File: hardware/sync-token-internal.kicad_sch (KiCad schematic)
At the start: 4 parts, among them U13 74AHC74, U18 74LVC2G125

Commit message: Switch part number for flip-flops
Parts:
- U13: JLCPCB Part Number C71900 -> C8179; Mouser Part Number 771-AHCPW118 -> 595-SN74AHC74PWR; Part Number 74AHC74PW,118 -> SN74AHC74PWR
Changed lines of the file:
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@@
 			)
 		)
-		(property "Datasheet" "https://www.mouser.com/datasheet/2/916/74AHC_AHCT74-2937188.pdf"
+		(property "Datasheet" "https://www.ti.com/lit/gpn/sn74ahc74"
 			(at 52.07 144.78 0)
 			(effects
@@
 			)
 		)
-		(property "Mouser Part Number" "771-AHCPW118"
+		(property "Mouser Part Number" "595-SN74AHC74PWR"
 			(at 52.07 144.78 0)
 			(effects
@@
 			)
 		)
-		(property "Part Number" "74AHC74PW,118"
+		(property "Part Number" "SN74AHC74PWR"
 			(at 52.07 144.78 0)
 			(effects
@@
 			)
 		)
-		(property "JLCPCB Part Number" "C71900"
+		(property "JLCPCB Part Number" "C8179"
 			(at 52.07 144.78 0)
 			(effects
@@
 			)
 		)
-		(property "Datasheet" "https://www.mouser.com/datasheet/2/916/74AHC_AHCT74-2937188.pdf"
+		(property "Datasheet" "https://www.ti.com/lit/gpn/sn74ahc74"
 			(at 187.96 111.76 0)
 			(effects
@@
 			)
 		)
-		(property "Mouser Part Number" "771-AHCPW118"
-			(at 187.96 111.76 0)
-			(effects
-				(font
-					(size 1.27 1.27)
-				)
-				(hide yes)
-			)
-		)
-		(property "Part Number" "74AHC74PW,118"
-			(at 187.96 111.76 0)
-			(effects
-				(font
-					(size 1.27 1.27)
-				)
-				(hide yes)
-			)
-		)
-		(property "JLCPCB Part Number" "C71900"
+		(property "Mouser Part Number" "595-SN74AHC74PWR"
+			(at 187.96 111.76 0)
+			(effects
+				(font
+					(size 1.27 1.27)
+				)
+				(hide yes)
+			)
+		)
+		(property "Part Number" "SN74AHC74PWR"
+			(at 187.96 111.76 0)
+			(effects
+				(font
+					(size 1.27 1.27)
+				)
+				(hide yes)
+			)
+		)
+		(property "JLCPCB Part Number" "C8179"
 			(at 187.96 111.76 0)
 			(effects
@@
 			)
 		)
-		(property "Datasheet" "https://www.mouser.com/datasheet/2/916/74AHC_AHCT74-2937188.pdf"
+		(property "Datasheet" "https://www.ti.com/lit/gpn/sn74ahc74"
 			(at 53.34 93.98 0)
 			(effects
@@
 			)
 		)
-		(property "Mouser Part Number" "771-AHCPW118"
-			(at 53.34 93.98 0)
-			(effects
-				(font
-					(size 1.27 1.27)
-				)
-				(hide yes)
-			)
-		)
-		(property "Part Number" "74AHC74PW,118"
-			(at 53.34 93.98 0)
-			(effects
-				(font
-					(size 1.27 1.27)
-				)
-				(hide yes)
-			)
-		)
-		(property "JLCPCB Part Number" "C71900"
-			(at 53.34 93.98 0)
-			(effects
+		(property "Mouser Part Number" "595-SN74AHC74PWR"
+			(at 53.34 93.98 0)
+			(effects
+				(font
+					(size 1.27 1.27)
+				)
+				(hide yes)
+			)
+		)
+		(property "Part Number" "SN74AHC74PWR"
+			(at 53.34 93.98 0)
+			(effects
+				(font
+					(size 1.27 1.27)
+				)
+				(hide yes)
+			)
+		)
+		(property "JLCPCB Part Number" "C8179"
+			(at 53.34 93.98 0)
+			(effects

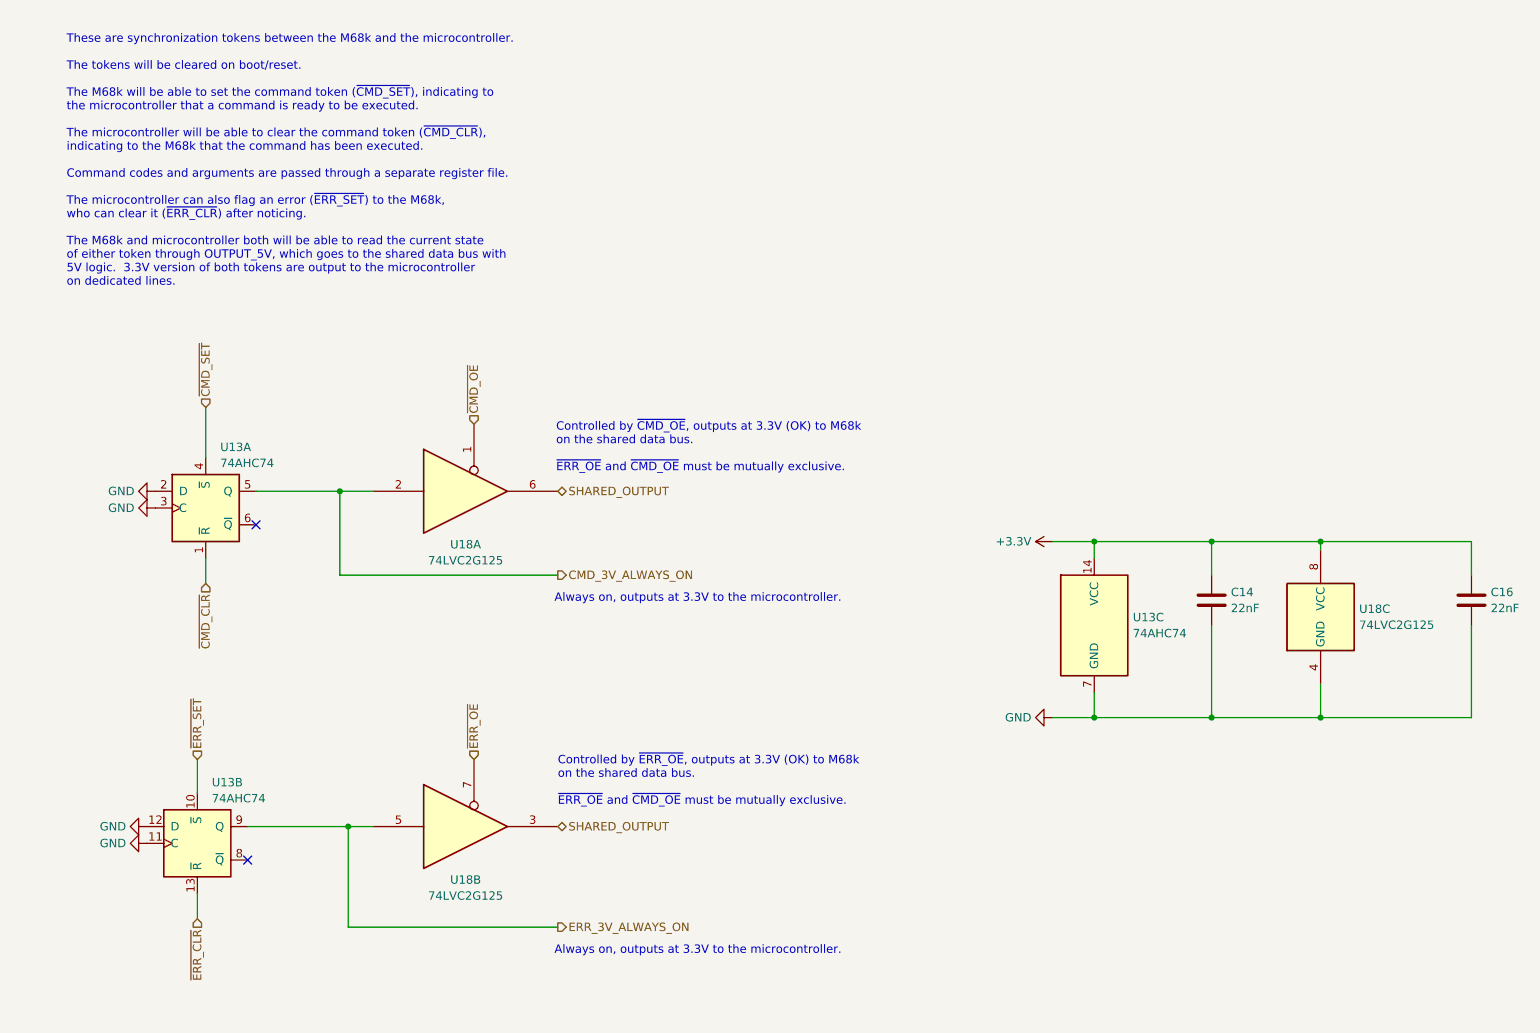
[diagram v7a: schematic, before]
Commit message: Move microcontroller board design into shareable subsheet
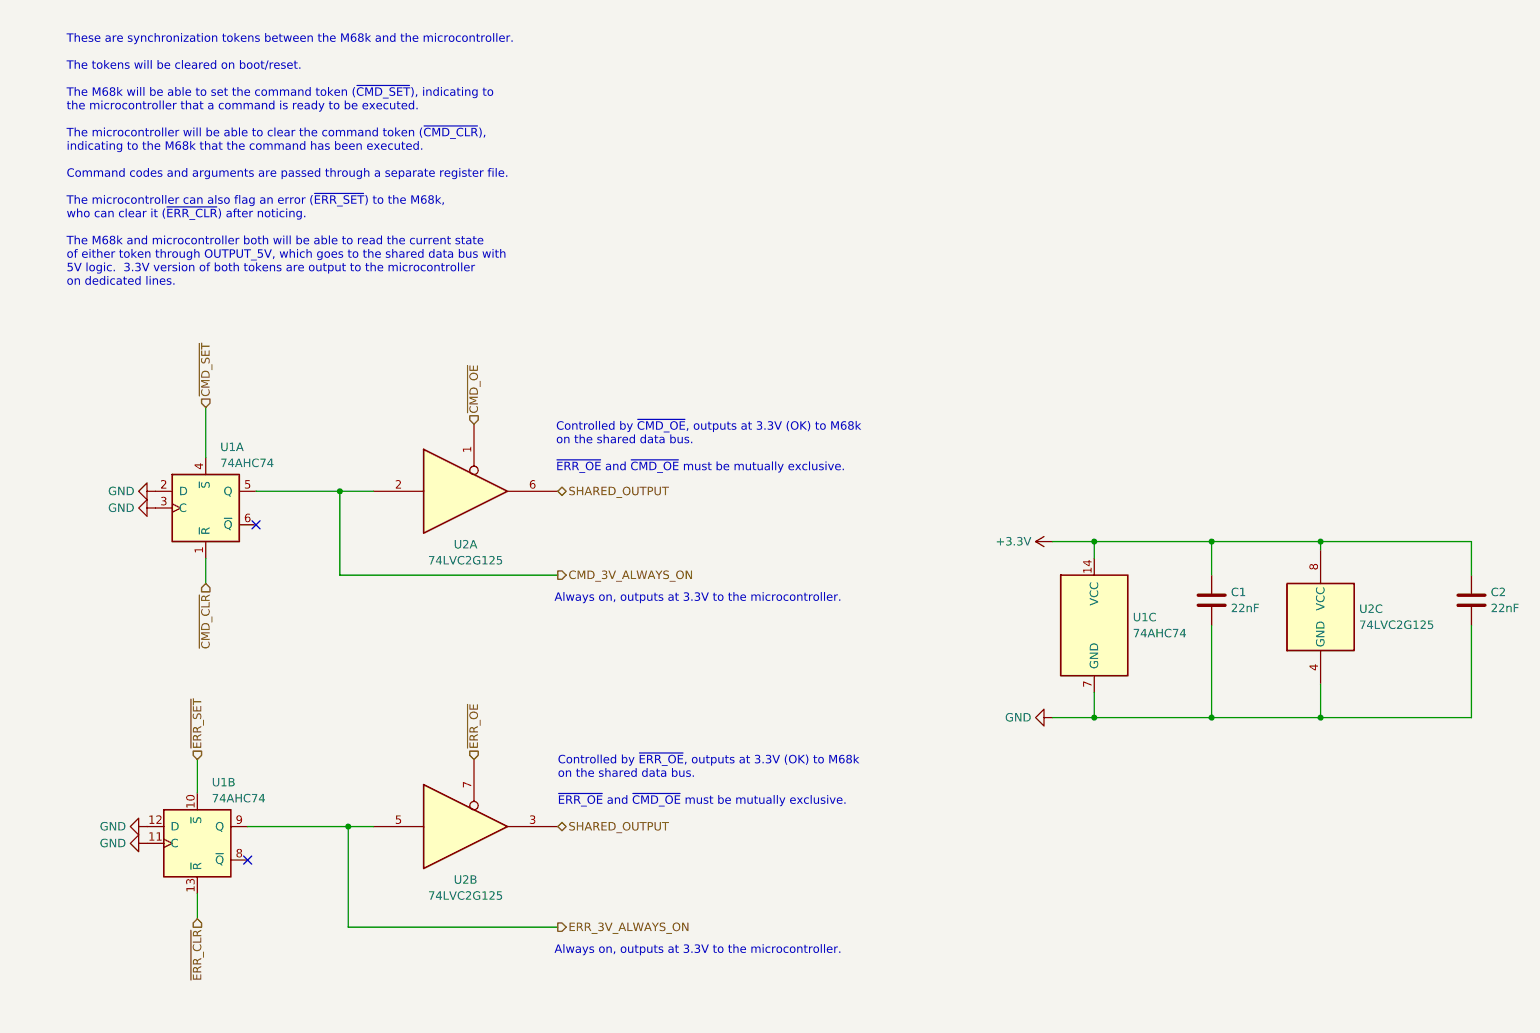
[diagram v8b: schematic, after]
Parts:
- renumbered C14 to C1, C16 to C2, U13 to U1, U18 to U2
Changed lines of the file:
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@@
 		(dnp no)
 		(fields_autoplaced yes)
-		(property "Reference" "U18"
+		(property "Reference" "U2"
 			(at 92.71 99.5101 0)
 			(effects
@@
 		)
 		(instances
-			(project ""
-				(path "/eb0e957f-b2ea-4261-97c1-e28148a3f6e1/fae06e8c-0a24-478c-87ed-aff0b09d1b33"
-					(reference "U18")
+			(project "microcontroller"
+				(path "/eb0e957f-b2ea-4261-97c1-e28148a3f6e1/1f234c04-2a4a-4cc4-8cff-97e40dff5b3b/2d231838-6b64-4e52-8f19-d0e449327717"
+					(reference "U2")
 					(unit 1)
 				)
@@
 		(dnp no)
 		(fields_autoplaced yes)
-		(property "Reference" "U18"
+		(property "Reference" "U2"
 			(at 92.71 150.3101 0)
 			(effects
@@
 		)
 		(instances
-			(project ""
-				(path "/eb0e957f-b2ea-4261-97c1-e28148a3f6e1/fae06e8c-0a24-478c-87ed-aff0b09d1b33"
-					(reference "U18")
+			(project "microcontroller"
+				(path "/eb0e957f-b2ea-4261-97c1-e28148a3f6e1/1f234c04-2a4a-4cc4-8cff-97e40dff5b3b/2d231838-6b64-4e52-8f19-d0e449327717"
+					(reference "U2")
 					(unit 2)
 				)
@@
 		(on_board yes)
 		(dnp no)
-		(property "Reference" "#PWR077"
+		(property "Reference" "#PWR012"
 			(at 38.1 144.78 0)
 			(effects
@@
 		(instances
 			(project "microcontroller"
-				(path "/eb0e957f-b2ea-4261-97c1-e28148a3f6e1/fae06e8c-0a24-478c-87ed-aff0b09d1b33"
-					(reference "#PWR077")
+				(path "/eb0e957f-b2ea-4261-97c1-e28148a3f6e1/1f234c04-2a4a-4cc4-8cff-97e40dff5b3b/2d231838-6b64-4e52-8f19-d0e449327717"
+					(reference "#PWR012")
 					(unit 1)
 				)
@@
 		(dnp no)
 		(fields_autoplaced yes)
-		(property "Reference" "C14"
+		(property "Reference" "C1"
 			(at 208.661 106.7378 0)
 			(effects
@@
 		(instances
 			(project "microcontroller"
-				(path "/eb0e957f-b2ea-4261-97c1-e28148a3f6e1/fae06e8c-0a24-478c-87ed-aff0b09d1b33"
-					(reference "C14")
+				(path "/eb0e957f-b2ea-4261-97c1-e28148a3f6e1/1f234c04-2a4a-4cc4-8cff-97e40dff5b3b/2d231838-6b64-4e52-8f19-d0e449327717"
+					(reference "C1")
 					(unit 1)
 				)
@@
 		(dnp no)
 		(fields_autoplaced yes)
-		(property "Reference" "U18"
+		(property "Reference" "U2"
 			(at 228.092 109.2778 0)
 			(effects
@@
 		)
 		(instances
-			(project ""
-				(path "/eb0e957f-b2ea-4261-97c1-e28148a3f6e1/fae06e8c-0a24-478c-87ed-aff0b09d1b33"
-					(reference "U18")
+			(project "microcontroller"
+				(path "/eb0e957f-b2ea-4261-97c1-e28148a3f6e1/1f234c04-2a4a-4cc4-8cff-97e40dff5b3b/2d231838-6b64-4e52-8f19-d0e449327717"
+					(reference "U2")
 					(unit 3)
 				)
@@
 		(dnp no)
 		(fields_autoplaced yes)
-		(property "Reference" "U13"
+		(property "Reference" "U1"
 			(at 54.2641 135.5555 0)
 			(effects
@@
 		(instances
 			(project "microcontroller"
-				(path "/eb0e957f-b2ea-4261-97c1-e28148a3f6e1/fae06e8c-0a24-478c-87ed-aff0b09d1b33"
-					(reference "U13")
+				(path "/eb0e957f-b2ea-4261-97c1-e28148a3f6e1/1f234c04-2a4a-4cc4-8cff-97e40dff5b3b/2d231838-6b64-4e52-8f19-d0e449327717"
+					(reference "U1")
 					(unit 2)
 				)
@@
 		(dnp no)
 		(fields_autoplaced yes)
-		(property "Reference" "#PWR080"
+		(property "Reference" "#PWR016"
 			(at 175.26 125.73 0)
 			(effects
@@
 		(instances
 			(project "microcontroller"
-				(path "/eb0e957f-b2ea-4261-97c1-e28148a3f6e1/fae06e8c-0a24-478c-87ed-aff0b09d1b33"
-					(reference "#PWR080")
+				(path "/eb0e957f-b2ea-4261-97c1-e28148a3f6e1/1f234c04-2a4a-4cc4-8cff-97e40dff5b3b/2d231838-6b64-4e52-8f19-d0e449327717"
+					(reference "#PWR016")
 					(unit 1)
 				)
@@
 		(dnp no)
 		(fields_autoplaced yes)
-		(property "Reference" "U13"
+		(property "Reference" "U1"
 			(at 193.802 110.5478 0)
 			(effects
@@
 		(instances
 			(project "microcontroller"
-				(path "/eb0e957f-b2ea-4261-97c1-e28148a3f6e1/fae06e8c-0a24-478c-87ed-aff0b09d1b33"
-					(reference "U13")
+				(path "/eb0e957f-b2ea-4261-97c1-e28148a3f6e1/1f234c04-2a4a-4cc4-8cff-97e40dff5b3b/2d231838-6b64-4e52-8f19-d0e449327717"
+					(reference "U1")
 					(unit 3)
 				)
@@
 		(dnp no)
 		(fields_autoplaced yes)
-		(property "Reference" "C16"
+		(property "Reference" "C2"
 			(at 248.031 106.7378 0)
 			(effects
@@
 		(instances
 			(project "microcontroller"
-				(path "/eb0e957f-b2ea-4261-97c1-e28148a3f6e1/fae06e8c-0a24-478c-87ed-aff0b09d1b33"
-					(reference "C16")
+				(path "/eb0e957f-b2ea-4261-97c1-e28148a3f6e1/1f234c04-2a4a-4cc4-8cff-97e40dff5b3b/2d231838-6b64-4e52-8f19-d0e449327717"
+					(reference "C2")
 					(unit 1)
 				)
@@
 		(dnp no)
 		(fields_autoplaced yes)
-		(property "Reference" "U13"
+		(property "Reference" "U1"
 			(at 55.5341 84.7555 0)
 			(effects
@@
 		(instances
 			(project "microcontroller"
-				(path "/eb0e957f-b2ea-4261-97c1-e28148a3f6e1/fae06e8c-0a24-478c-87ed-aff0b09d1b33"
-					(reference "U13")
+				(path "/eb0e957f-b2ea-4261-97c1-e28148a3f6e1/1f234c04-2a4a-4cc4-8cff-97e40dff5b3b/2d231838-6b64-4e52-8f19-d0e449327717"
+					(reference "U1")
 					(unit 1)
 				)
@@
 		(on_board yes)
 		(dnp no)
-		(property "Reference" "#PWR076"
+		(property "Reference" "#PWR03"
 			(at 38.1 142.24 0)
 			(effects
@@
 		(instances
 			(project "microcontroller"
-				(path "/eb0e957f-b2ea-4261-97c1-e28148a3f6e1/fae06e8c-0a24-478c-87ed-aff0b09d1b33"
-					(reference "#PWR076")
+				(path "/eb0e957f-b2ea-4261-97c1-e28148a3f6e1/1f234c04-2a4a-4cc4-8cff-97e40dff5b3b/2d231838-6b64-4e52-8f19-d0e449327717"
+					(reference "#PWR03")
 					(unit 1)
 				)
@@
 		(dnp no)
 		(fields_autoplaced yes)
-		(property "Reference" "#PWR078"
+		(property "Reference" "#PWR013"
 			(at 39.37 91.44 0)
 			(effects
@@
 		(instances
 			(project "microcontroller"
-				(path "/eb0e957f-b2ea-4261-97c1-e28148a3f6e1/fae06e8c-0a24-478c-87ed-aff0b09d1b33"
-					(reference "#PWR078")
+				(path "/eb0e957f-b2ea-4261-97c1-e28148a3f6e1/1f234c04-2a4a-4cc4-8cff-97e40dff5b3b/2d231838-6b64-4e52-8f19-d0e449327717"
+					(reference "#PWR013")
 					(unit 1)
 				)
@@
 		(dnp no)
 		(fields_autoplaced yes)
-		(property "Reference" "#PWR079"
+		(property "Reference" "#PWR014"
 			(at 39.37 93.98 0)
 			(effects
@@
 		(instances
 			(project "microcontroller"
-				(path "/eb0e957f-b2ea-4261-97c1-e28148a3f6e1/fae06e8c-0a24-478c-87ed-aff0b09d1b33"
-					(reference "#PWR079")
+				(path "/eb0e957f-b2ea-4261-97c1-e28148a3f6e1/1f234c04-2a4a-4cc4-8cff-97e40dff5b3b/2d231838-6b64-4e52-8f19-d0e449327717"
+					(reference "#PWR014")
 					(unit 1)
 				)
@@
 		(dnp no)
 		(fields_autoplaced yes)
-		(property "Reference" "#PWR069"
+		(property "Reference" "#PWR015"
 			(at 185.42 99.06 0)
 			(effects
@@
 		(instances
 			(project "microcontroller"
-				(path "/eb0e957f-b2ea-4261-97c1-e28148a3f6e1/fae06e8c-0a24-478c-87ed-aff0b09d1b33"
-					(reference "#PWR069")
+				(path "/eb0e957f-b2ea-4261-97c1-e28148a3f6e1/1f234c04-2a4a-4cc4-8cff-97e40dff5b3b/2d231838-6b64-4e52-8f19-d0e449327717"
+					(reference "#PWR015")
 					(unit 1)
 				)
